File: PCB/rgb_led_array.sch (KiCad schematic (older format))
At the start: 2 parts, among them U2 TLC5955DCA

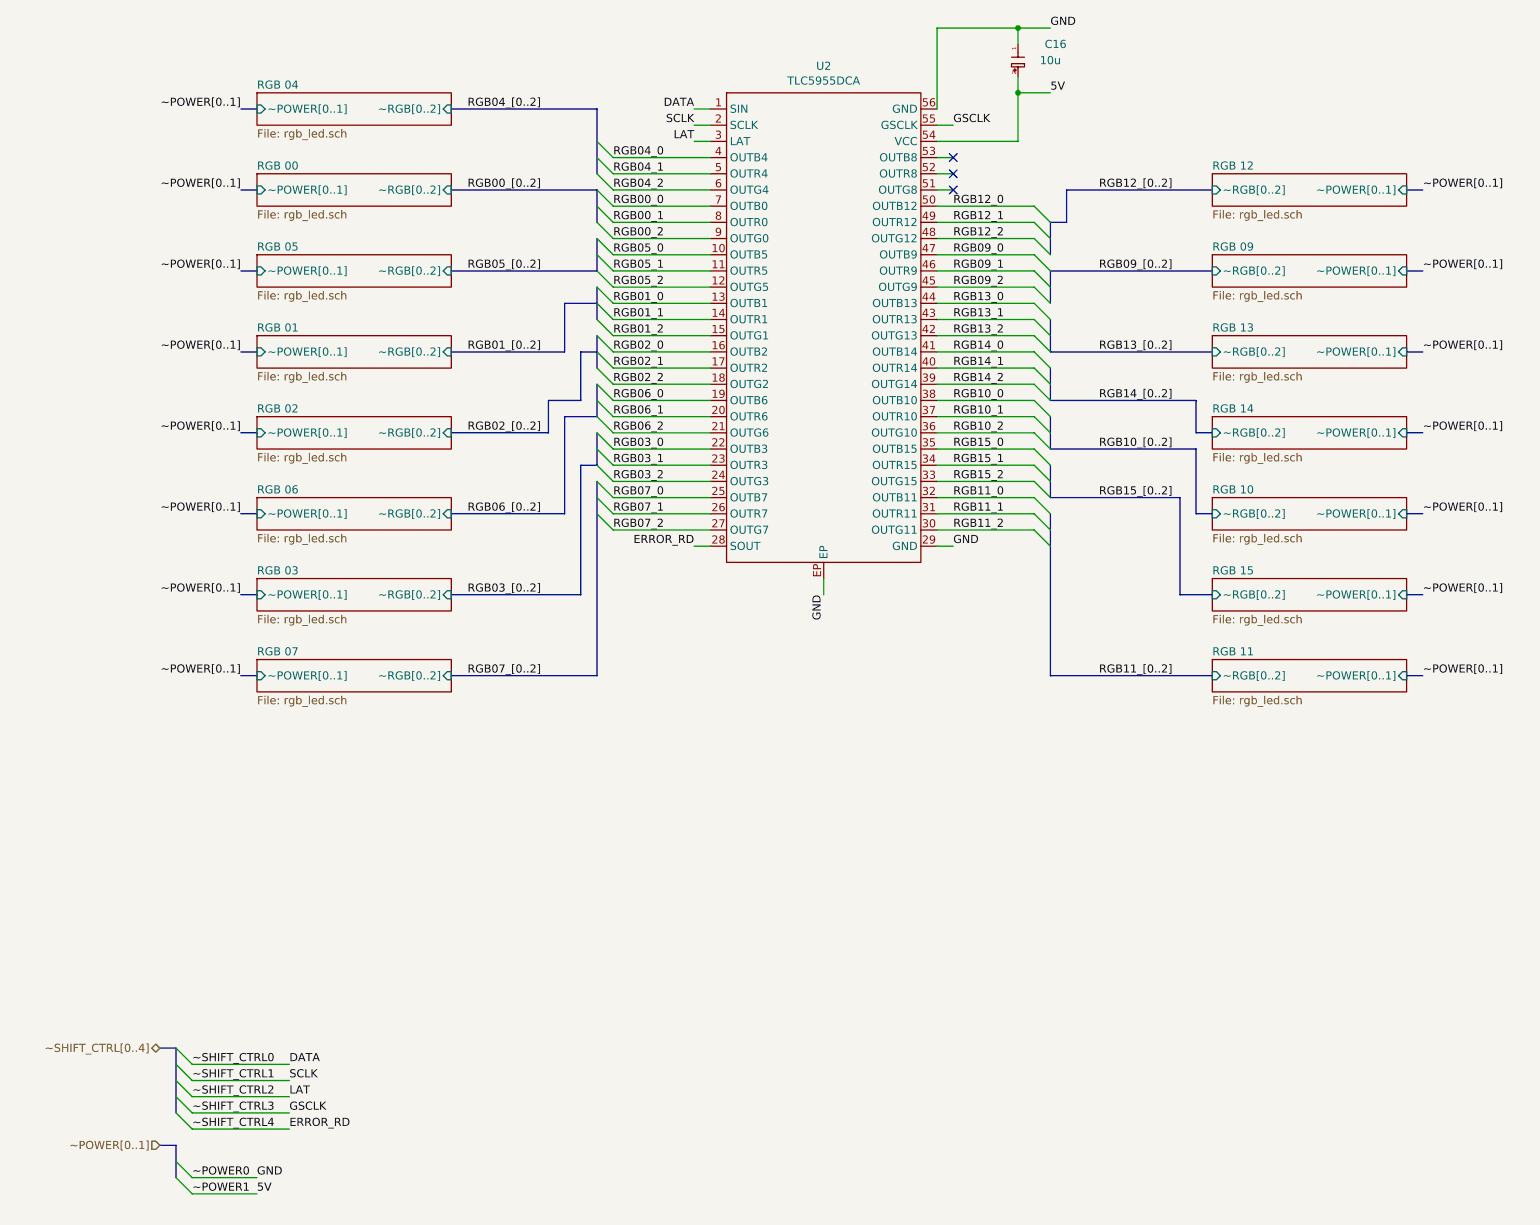
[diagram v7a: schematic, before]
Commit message: Removed Level Shifter, Cleaned up gerbers
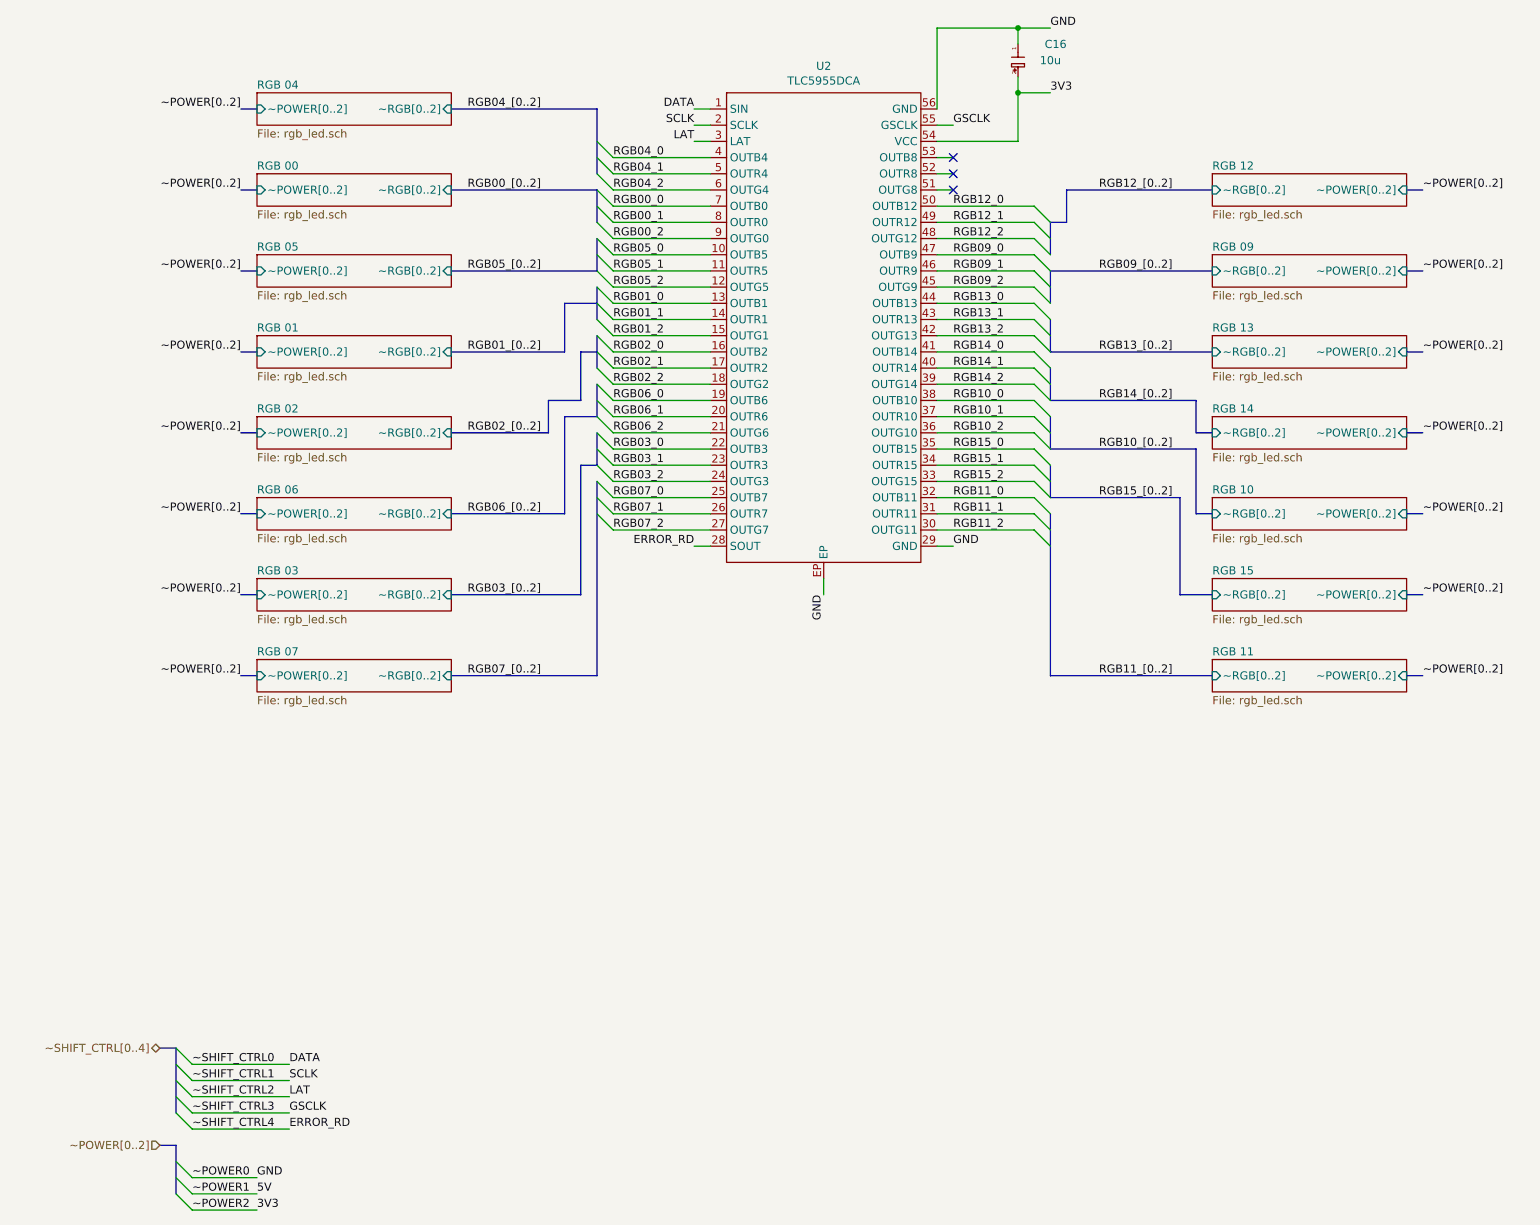
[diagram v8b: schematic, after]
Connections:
- net 5V: no longer C16.2, U2.54 (VCC)
- new net 3V3: C16.2, U2.54 (VCC)
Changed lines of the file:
@@
 Sheet 4 20
 Title "Christmas Tree Disco"
-Date "2017-08-15"
+Date "2017-08-23"
 Rev "V1.0"
 Comp "www.GitHub.com/Cryochasm"
@@
 F1 "rgb_led.sch" 50
 F2 "~~RGB[0..2]" I R 3100 1600 50
-F3 "~~POWER[0..1]" I L 1900 1600 50
+F3 "~~POWER[0..2]" I L 1900 1600 50
 $EndSheet
 $Comp
@@
 F1 "rgb_led.sch" 50
 F2 "~~RGB[0..2]" I R 3100 1100 50
-F3 "~~POWER[0..1]" I L 1900 1100 50
+F3 "~~POWER[0..2]" I L 1900 1100 50
 $EndSheet
 Wire Bus Line
@@
 F1 "rgb_led.sch" 50
 F2 "~~RGB[0..2]" I R 3100 2100 50
-F3 "~~POWER[0..1]" I L 1900 2100 50
+F3 "~~POWER[0..2]" I L 1900 2100 50
 $EndSheet
 $Sheet
@@
 F1 "rgb_led.sch" 50
 F2 "~~RGB[0..2]" I R 3100 3100 50
-F3 "~~POWER[0..1]" I L 1900 3100 50
+F3 "~~POWER[0..2]" I L 1900 3100 50
 $EndSheet
 $Sheet
@@
 F1 "rgb_led.sch" 50
 F2 "~~RGB[0..2]" I R 3100 4100 50
-F3 "~~POWER[0..1]" I L 1900 4100 50
+F3 "~~POWER[0..2]" I L 1900 4100 50
 $EndSheet
 $Sheet
@@
 F1 "rgb_led.sch" 50
 F2 "~~RGB[0..2]" I R 3100 3600 50
-F3 "~~POWER[0..1]" I L 1900 3600 50
+F3 "~~POWER[0..2]" I L 1900 3600 50
 $EndSheet
 $Sheet
@@
 F1 "rgb_led.sch" 50
 F2 "~~RGB[0..2]" I R 3100 4600 50
-F3 "~~POWER[0..1]" I L 1900 4600 50
+F3 "~~POWER[0..2]" I L 1900 4600 50
 $EndSheet
 Wire Bus Line
@@
 F1 "rgb_led.sch" 50
 F2 "~~RGB[0..2]" I R 3100 2600 50
-F3 "~~POWER[0..1]" I L 1900 2600 50
+F3 "~~POWER[0..2]" I L 1900 2600 50
 $EndSheet
 Wire Bus Line
@@
 F1 "rgb_led.sch" 50
 F2 "~~RGB[0..2]" I L 7800 1600 50
-F3 "~~POWER[0..1]" I R 9000 1600 50
+F3 "~~POWER[0..2]" I R 9000 1600 50
 $EndSheet
 $Sheet
@@
 F1 "rgb_led.sch" 50
 F2 "~~RGB[0..2]" I L 7800 2100 50
-F3 "~~POWER[0..1]" I R 9000 2100 50
+F3 "~~POWER[0..2]" I R 9000 2100 50
 $EndSheet
 $Sheet
@@
 F1 "rgb_led.sch" 50
 F2 "~~RGB[0..2]" I L 7800 2600 50
-F3 "~~POWER[0..1]" I R 9000 2600 50
+F3 "~~POWER[0..2]" I R 9000 2600 50
 $EndSheet
 $Sheet
@@
 F1 "rgb_led.sch" 50
 F2 "~~RGB[0..2]" I L 7800 3100 50
-F3 "~~POWER[0..1]" I R 9000 3100 50
+F3 "~~POWER[0..2]" I R 9000 3100 50
 $EndSheet
 $Sheet
@@
 F1 "rgb_led.sch" 50
 F2 "~~RGB[0..2]" I L 7800 3600 50
-F3 "~~POWER[0..1]" I R 9000 3600 50
+F3 "~~POWER[0..2]" I R 9000 3600 50
 $EndSheet
 $Sheet
@@
 F1 "rgb_led.sch" 50
 F2 "~~RGB[0..2]" I L 7800 4100 50
-F3 "~~POWER[0..1]" I R 9000 4100 50
+F3 "~~POWER[0..2]" I R 9000 4100 50
 $EndSheet
 $Sheet
@@
 F1 "rgb_led.sch" 50
 F2 "~~RGB[0..2]" I L 7800 4600 50
-F3 "~~POWER[0..1]" I R 9000 4600 50
+F3 "~~POWER[0..2]" I R 9000 4600 50
 $EndSheet
 Wire Bus Line
@@
 	6100 1200 6200 1200
 Text HLabel 1300 7500 0    50   Input ~ 0
-~~POWER[0..1]
+~~POWER[0..2]
 Wire Bus Line
 	1300 7500 1400 7500
 Wire Bus Line
-	1400 7500 1400 7700
+	1400 7500 1400 7800
 Entry Wire Line
 	1400 7600 1500 7700
@@
 Text Label 6800 600  0    50   ~ 0
 GND
-Text Label 6800 1000 0    50   ~ 0
-5V
 Text HLabel 1300 6900 0    50   BiDi ~ 0
 ~~SHIFT_CTRL[0..4]
@@
 	1900 4600 1800 4600
 Text Label 1800 4600 2    50   ~ 0
-~~POWER[0..1]
+~~POWER[0..2]
 Wire Bus Line
 	1900 4100 1800 4100
 Text Label 1800 4100 2    50   ~ 0
-~~POWER[0..1]
+~~POWER[0..2]
 Wire Bus Line
 	1900 3600 1800 3600
 Text Label 1800 3600 2    50   ~ 0
-~~POWER[0..1]
+~~POWER[0..2]
 Wire Bus Line
 	1900 3100 1800 3100
 Text Label 1800 3100 2    50   ~ 0
-~~POWER[0..1]
+~~POWER[0..2]
 Wire Bus Line
 	1900 2600 1800 2600
 Text Label 1800 2600 2    50   ~ 0
-~~POWER[0..1]
+~~POWER[0..2]
 Wire Bus Line
 	1900 2100 1800 2100
 Text Label 1800 2100 2    50   ~ 0
-~~POWER[0..1]
+~~POWER[0..2]
 Wire Bus Line
 	1900 1600 1800 1600
 Text Label 1800 1600 2    50   ~ 0
-~~POWER[0..1]
+~~POWER[0..2]
 Wire Bus Line
 	1900 1100 1800 1100
 Text Label 1800 1100 2    50   ~ 0
-~~POWER[0..1]
+~~POWER[0..2]
 Text Label 9100 1600 0    50   ~ 0
-~~POWER[0..1]
+~~POWER[0..2]
 Text Label 9100 2100 0    50   ~ 0
-~~POWER[0..1]
+~~POWER[0..2]
 Text Label 9100 2600 0    50   ~ 0
-~~POWER[0..1]
+~~POWER[0..2]
 Text Label 9100 3100 0    50   ~ 0
-~~POWER[0..1]
+~~POWER[0..2]
 Text Label 9100 3600 0    50   ~ 0
-~~POWER[0..1]
+~~POWER[0..2]
 Text Label 9100 4100 0    50   ~ 0
-~~POWER[0..1]
+~~POWER[0..2]
 Text Label 9100 4600 0    50   ~ 0
-~~POWER[0..1]
+~~POWER[0..2]
 Wire Bus Line
 	9000 4600 9100 4600
@@
 	0    1    1    0
 $EndComp
+Entry Wire Line
+	1400 7800 1500 7900
+Text Label 1500 7900 0    50   ~ 0
+~~POWER2
+Wire Wire Line
+	1500 7900 1900 7900
+Text Label 1900 7900 0    50   ~ 0
+3V3
+Text Label 6800 1000 0    50   ~ 0
+3V3
 $EndSCHEMATC
